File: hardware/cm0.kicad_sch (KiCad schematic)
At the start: 0 parts

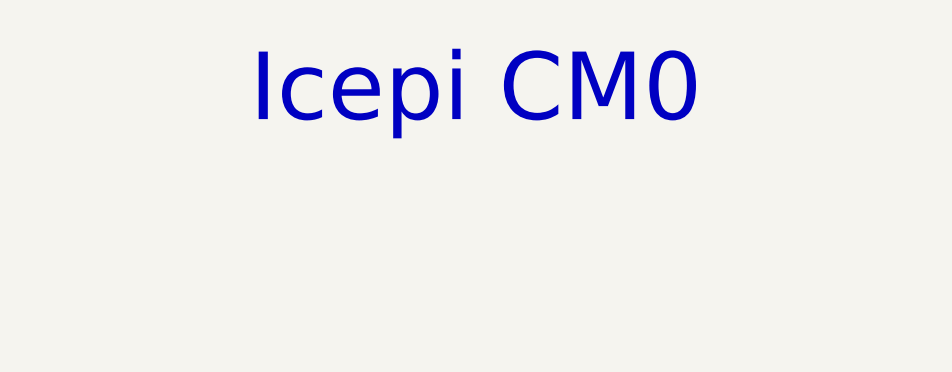
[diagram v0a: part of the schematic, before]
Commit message: Update crystal
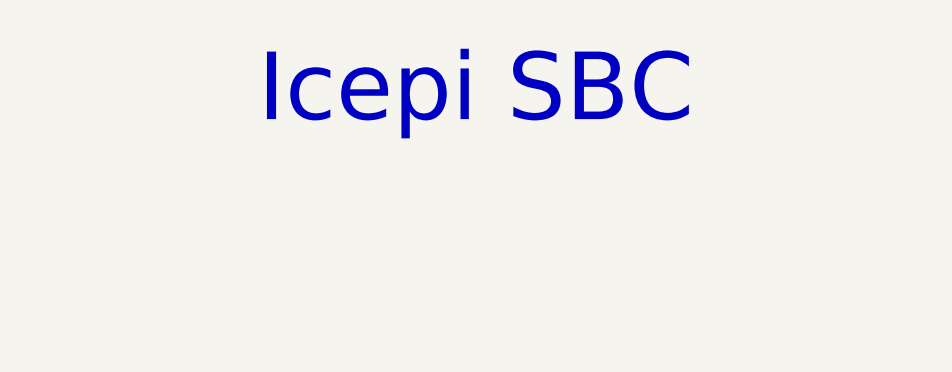
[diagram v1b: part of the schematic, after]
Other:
- note added: "Icepi SBC"
- note removed: "Icepi CM0"
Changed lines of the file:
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@@
 		)
 	)
-	(text "Icepi CM0"
+	(text "Icepi SBC"
 		(exclude_from_sim no)
 		(at 139.7 23.114 0)

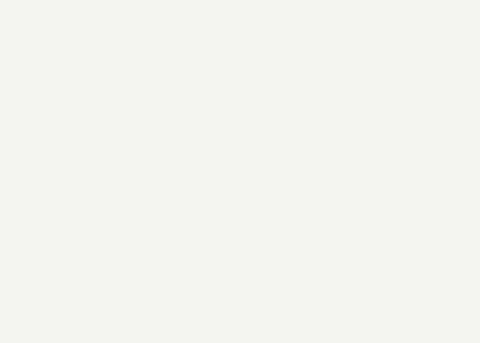
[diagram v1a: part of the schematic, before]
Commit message: Updated README and improved audio routing
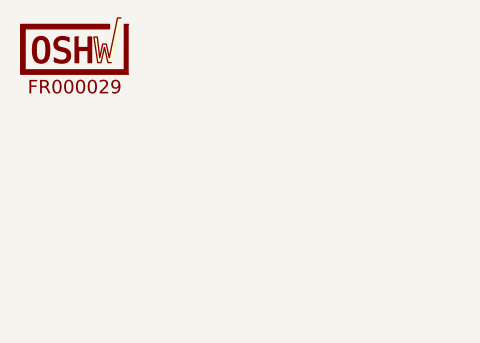
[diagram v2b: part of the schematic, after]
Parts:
- added LOGO1: ~, symbol oshwa:OSHW_Certification_Mark_Stacked_Medium
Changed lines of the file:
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@@
+		)
+	)
+	(symbol
+		(lib_id "oshwa:OSHW_Certification_Mark_Stacked_Medium")
+		(at 21.59 17.78 0)
+		(unit 1)
+		(exclude_from_sim no)
+		(in_bom no)
+		(on_board no)
+		(dnp no)
+		(fields_autoplaced yes)
+		(property "Reference" "LOGO1"
+			(at 43.18 35.56 0)
+			(effects
+				(font
+					(size 1.27 1.27)
+				)
+				(hide yes)
+			)
+		)
+		(property "Value" "~"
+			(at 43.18 35.56 0)
+			(effects
+				(font
+					(size 1.27 1.27)
+				)
+				(hide yes)
+			)
+		)
+		(property "Footprint" ""
+			(at 43.18 35.56 0)
+			(effects
+				(font
+					(size 1.27 1.27)
+				)
+				(hide yes)
+			)
+		)
+		(property "Datasheet" ""
+			(at 43.18 35.56 0)
+			(effects
+				(font
+					(size 1.27 1.27)
+				)
+				(hide yes)
+			)
+		)
+		(property "Description" "OSHW Certification Mark, Stacked"
+			(at 43.18 35.56 0)
+			(effects
+				(font
+					(size 1.27 1.27)
+				)
+				(hide yes)
+			)
+		)
+		(instances
+			(project ""
+				(path "/b53f5dbb-8078-4818-9e8f-fdf90ba6d854"
+					(reference "LOGO1")
+					(unit 1)
+				)
+				(path "/b53f5dbb-8078-4818-9e8f-fdf90ba6d854/f05ec484-f958-442a-a016-134b1e35dc2c"
+					(reference "LOGO1")
+					(unit 1)
+				)
+			)
 		)
 	)

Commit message: Add schematic pdf
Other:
- title: Icepi CM0 -> Icepi SBC
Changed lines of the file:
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@@
 	(paper "A4")
 	(title_block
-		(title "Icepi CM0")
-		(date "2025-11-21")
+		(title "Icepi SBC")
+		(date "2025-12-21")
 		(rev "v1.0")
 		(company "Icy Electronics")
 		(comment 1 "Chengyin Yao (cheyao)")
-		(comment 2 "https://github.com/cheyao/icepi-cm0")
+		(comment 2 "https://github.com/cheyao/icepi-sbc")
 		(comment 3 "License: Solderpad")
 	)
